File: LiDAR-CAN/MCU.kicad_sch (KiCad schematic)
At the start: 25 parts, among them J5 61300511121, SW1 RST, U5 STM32F401RBT6, Y3 25MHz

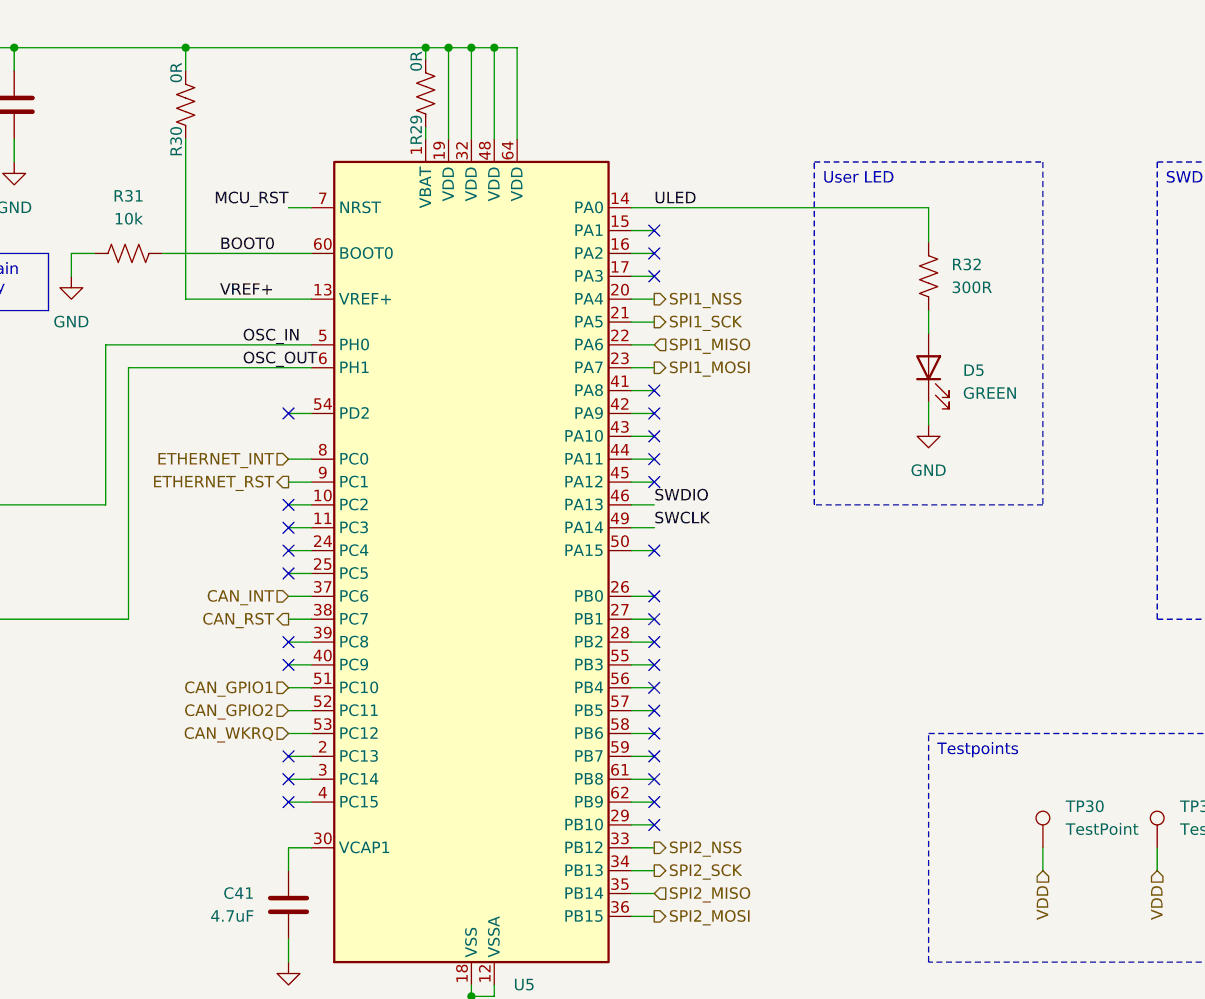
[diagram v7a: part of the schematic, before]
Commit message: Add CAN and MCU placement
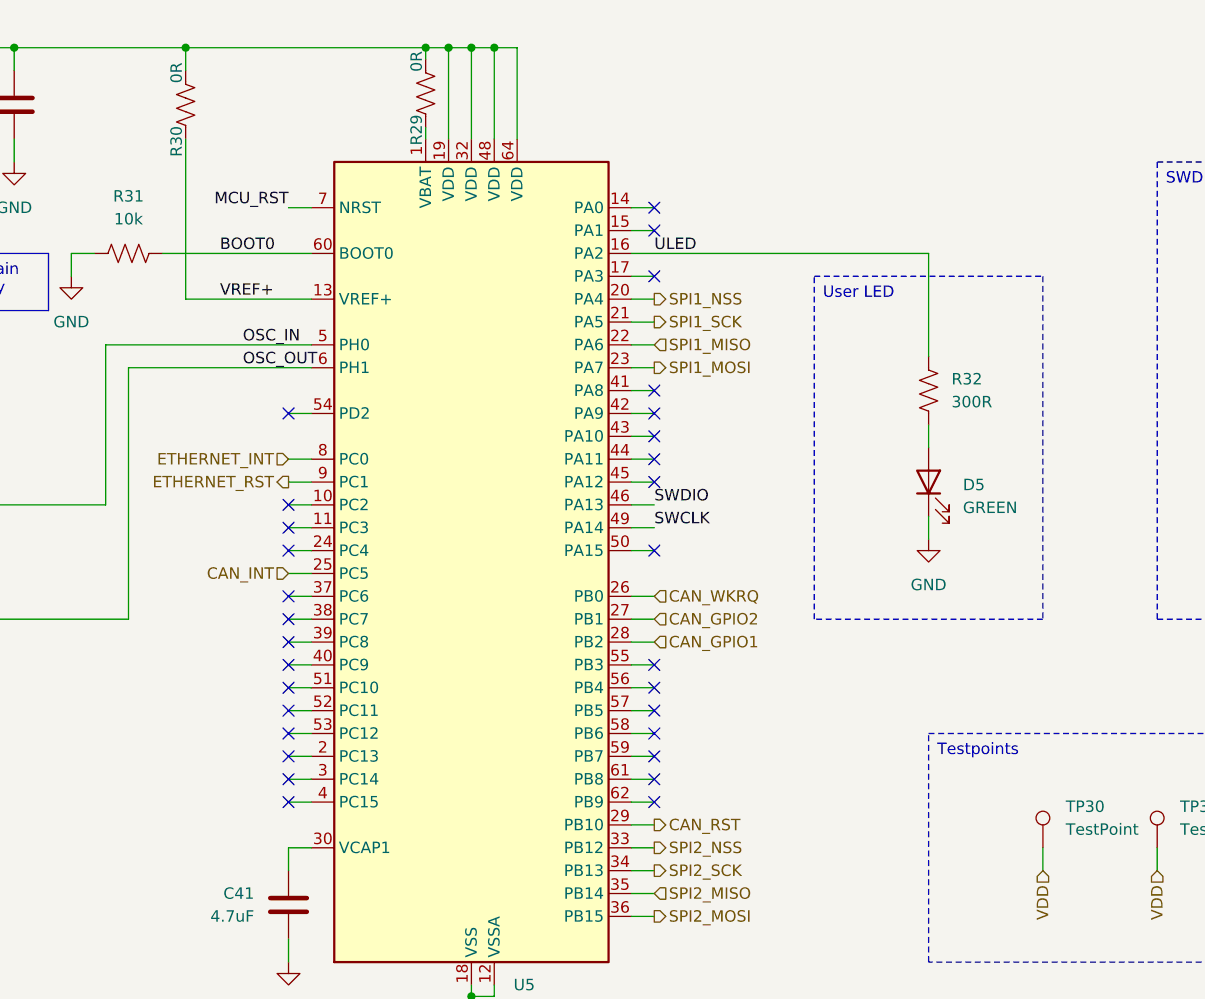
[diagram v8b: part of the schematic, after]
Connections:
- net CAN_GPIO1: now also U5.28 (PB2); no longer U5.51 (PC10)
- net CAN_GPIO2: now also U5.27 (PB1); no longer U5.52 (PC11)
- net CAN_INT: now also U5.25 (PC5); no longer U5.37 (PC6)
- net CAN_RST: now also U5.29 (PB10); no longer U5.38 (PC7)
- net CAN_WKRQ: now also U5.26 (PB0); no longer U5.53 (PC12)
- net ULED: now also U5.16 (PA2); no longer U5.14 (PA0)
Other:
- moved on the sheet: D5, R32
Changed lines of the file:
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@@
 	(text_box "User LED"
 		(exclude_from_sim no)
-		(at 190.5 50.8 0)
+		(at 190.5 63.5 0)
 		(size 25.4 38.1)
 		(margins 0.9525 0.9525 0.9525 0.9525)
@@
 	)
 	(no_connect
-		(at 172.72 99.06)
-	)
-	(no_connect
 		(at 132.08 119.38)
 	)
@@
 	)
 	(no_connect
+		(at 132.08 99.06)
+	)
+	(no_connect
 		(at 132.08 91.44)
 	)
@@
 	)
 	(no_connect
+		(at 132.08 101.6)
+	)
+	(no_connect
 		(at 132.08 78.74)
 	)
 	(no_connect
-		(at 172.72 124.46)
+		(at 172.72 55.88)
 	)
 	(no_connect
@@
 	)
 	(no_connect
-		(at 132.08 96.52)
-	)
-	(no_connect
-		(at 172.72 104.14)
-	)
-	(no_connect
-		(at 172.72 60.96)
+		(at 172.72 109.22)
 	)
 	(no_connect
-		(at 172.72 101.6)
+		(at 132.08 111.76)
 	)
 	(no_connect
-		(at 172.72 109.22)
+		(at 132.08 114.3)
 	)
 	(no_connect
@@
 	)
 	(no_connect
+		(at 132.08 109.22)
+	)
+	(no_connect
 		(at 172.72 78.74)
 	)
@@
 	(wire
 		(pts
-			(xy 170.18 55.88) (xy 203.2 55.88)
-		)
-		(stroke
-			(width 0)
-			(type default)
-		)
-	)
-	(wire
-		(pts
 			(xy 88.9 48.26) (xy 88.9 50.8)
 		)
@@
 	(wire
 		(pts
+			(xy 170.18 55.88) (xy 172.72 55.88)
+		)
+		(stroke
+			(width 0)
+			(type default)
+		)
+	)
+	(wire
+		(pts
 			(xy 77.47 95.25) (xy 77.47 104.14)
 		)
@@
 	(wire
 		(pts
+			(xy 203.2 60.96) (xy 203.2 72.39)
+		)
+		(stroke
+			(width 0)
+			(type default)
+		)
+	)
+	(wire
+		(pts
 			(xy 50.8 157.48) (xy 50.8 160.02)
 		)
@@
 	(wire
 		(pts
-			(xy 203.2 80.01) (xy 203.2 77.47)
+			(xy 203.2 92.71) (xy 203.2 90.17)
 		)
 		(stroke
@@
 	(wire
 		(pts
-			(xy 170.18 60.96) (xy 172.72 60.96)
+			(xy 170.18 60.96) (xy 203.2 60.96)
 		)
 		(stroke
@@
 	(wire
 		(pts
-			(xy 203.2 69.85) (xy 203.2 67.31)
+			(xy 203.2 82.55) (xy 203.2 80.01)
 		)
 		(stroke
@@
 	(wire
 		(pts
-			(xy 203.2 59.69) (xy 203.2 55.88)
-		)
-		(stroke
-			(width 0)
-			(type default)
-		)
-	)
-	(wire
-		(pts
 			(xy 111.76 88.9) (xy 73.66 88.9)
 		)
@@
 	)
 	(label "ULED"
-		(at 172.72 55.88 0)
+		(at 172.72 60.96 0)
 		(effects
 			(font
@@
 		)
 	)
-	(hierarchical_label "ETHERNET_RST"
-		(shape output)
-		(at 132.08 86.36 180)
-		(effects
-			(font
-				(size 1.27 1.27)
-			)
-			(justify right)
-		)
-	)
 	(hierarchical_label "CAN_GPIO2"
 		(shape input)
-		(at 132.08 111.76 180)
+		(at 172.72 101.6 0)
 		(effects
 			(font
 				(size 1.27 1.27)
 			)
-			(justify right)
+			(justify left)
 		)
 	)
-	(hierarchical_label "CAN_WKRQ"
-		(shape input)
-		(at 132.08 114.3 180)
+	(hierarchical_label "ETHERNET_RST"
+		(shape output)
+		(at 132.08 86.36 180)
 		(effects
 			(font
@@
 		)
 	)
+	(hierarchical_label "CAN_WKRQ"
+		(shape input)
+		(at 172.72 99.06 0)
+		(effects
+			(font
+				(size 1.27 1.27)
+			)
+			(justify left)
+		)
+	)
 	(hierarchical_label "CAN_GPIO1"
 		(shape input)
-		(at 132.08 109.22 180)
+		(at 172.72 104.14 0)
 		(effects
 			(font
 				(size 1.27 1.27)
 			)
-			(justify right)
+			(justify left)
 		)
 	)
@@
 		)
 	)
-	(hierarchical_label "CAN_INT"
-		(shape input)
-		(at 132.08 99.06 180)
+	(hierarchical_label "CAN_RST"
+		(shape output)
+		(at 172.72 124.46 0)
 		(effects
 			(font
 				(size 1.27 1.27)
 			)
-			(justify right)
+			(justify left)
 		)
 	)
@@
 		)
 	)
+	(hierarchical_label "CAN_INT"
+		(shape input)
+		(at 132.08 96.52 180)
+		(effects
+			(font
+				(size 1.27 1.27)
+			)
+			(justify right)
+		)
+	)
 	(hierarchical_label "SPI1_MOSI"
 		(shape output)
@@
 		)
 	)
-	(hierarchical_label "CAN_RST"
-		(shape output)
-		(at 132.08 101.6 180)
-		(effects
-			(font
-				(size 1.27 1.27)
-			)
-			(justify right)
-		)
-	)
 	(symbol
 		(lib_id "power:GND")
@@
 	(symbol
 		(lib_id "Device:LED")
-		(at 203.2 73.66 90)
+		(at 203.2 86.36 90)
 		(unit 1)
 		(exclude_from_sim no)
@@
 		(fields_autoplaced yes)
 		(property "Reference" "D5"
-			(at 207.01 73.9774 90)
+			(at 207.01 86.6774 90)
 			(effects
 				(font
@@
 		)
 		(property "Value" "GREEN"
-			(at 207.01 76.5174 90)
+			(at 207.01 89.2174 90)
 			(effects
 				(font
@@
 		)
 		(property "Footprint" "LED_SMD:LED_0603_1608Metric"
-			(at 203.2 73.66 0)
+			(at 203.2 86.36 0)
 			(effects
 				(font
@@
 		)
 		(property "Datasheet" "https://mm.digikey.com/Volume0/opasdata/d220001/medias/docus/858/LTST-C190GKT.pdf"
-			(at 203.2 73.66 0)
+			(at 203.2 86.36 0)
 			(effects
 				(font
@@
 		)
 		(property "Description" "LED GREEN CLEAR CHIP SMD 0603"
-			(at 203.2 73.66 0)
+			(at 203.2 86.36 0)
 			(effects
 				(font
@@
 		)
 		(property "Manufacturer" "Lite-On Inc."
-			(at 203.2 73.66 90)
+			(at 203.2 86.36 90)
 			(effects
 				(font
@@
 		)
 		(property "MPN" "LTST-C190GKT"
-			(at 203.2 73.66 90)
+			(at 203.2 86.36 90)
 			(effects
 				(font
@@
 	(symbol
 		(lib_id "Device:R_US")
-		(at 203.2 63.5 0)
+		(at 203.2 76.2 0)
 		(unit 1)
 		(exclude_from_sim no)
@@
 		(fields_autoplaced yes)
 		(property "Reference" "R32"
-			(at 205.74 62.2299 0)
+			(at 205.74 74.9299 0)
 			(effects
 				(font
@@
 		)
 		(property "Value" "300R"
-			(at 205.74 64.7699 0)
+			(at 205.74 77.4699 0)
 			(effects
 				(font
@@
 		)
 		(property "Footprint" "Resistor_SMD:R_0603_1608Metric"
-			(at 204.216 63.754 90)
+			(at 204.216 76.454 90)
 			(effects
 				(font
@@
 		)
 		(property "Datasheet" "https://www.yageo.com/upload/media/product/products/datasheet/rchip/PYu-RC_Group_51_RoHS_L_12.pdf"
-			(at 203.2 63.5 0)
+			(at 203.2 76.2 0)
 			(effects
 				(font
@@
 		)
 		(property "Description" "RES 300 OHM 5% 1/10W 0603"
-			(at 203.2 63.5 0)
+			(at 203.2 76.2 0)
 			(effects
 				(font
@@
 		)
 		(property "Manufacturer" "YAGEO"
-			(at 203.2 63.5 0)
+			(at 203.2 76.2 0)
 			(effects
 				(font
@@
 		)
 		(property "MPN" "RC0603JR-07300RL"
-			(at 203.2 63.5 0)
+			(at 203.2 76.2 0)
 			(effects
 				(font
@@
 	(symbol
 		(lib_id "power:GND")
-		(at 203.2 80.01 0)
+		(at 203.2 92.71 0)
 		(unit 1)
 		(exclude_from_sim no)
@@
 		(fields_autoplaced yes)
 		(property "Reference" "#PWR069"
-			(at 203.2 86.36 0)
+			(at 203.2 99.06 0)
 			(effects
 				(font
@@
 		)
 		(property "Value" "GND"
-			(at 203.2 85.09 0)
+			(at 203.2 97.79 0)
 			(effects
 				(font
@@
 		)
 		(property "Footprint" ""
-			(at 203.2 80.01 0)
+			(at 203.2 92.71 0)
 			(effects
 				(font
@@
 		)
 		(property "Datasheet" ""
-			(at 203.2 80.01 0)
+			(at 203.2 92.71 0)
 			(effects
 				(font
@@
 		)
 		(property "Description" "Power symbol creates a global label with name \"GND\" , ground"
-			(at 203.2 80.01 0)
+			(at 203.2 92.71 0)
 			(effects
 				(font
